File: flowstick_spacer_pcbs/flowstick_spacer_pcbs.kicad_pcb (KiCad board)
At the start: 2 copper layers, 13.6 x 40.4 mm, 0 parts

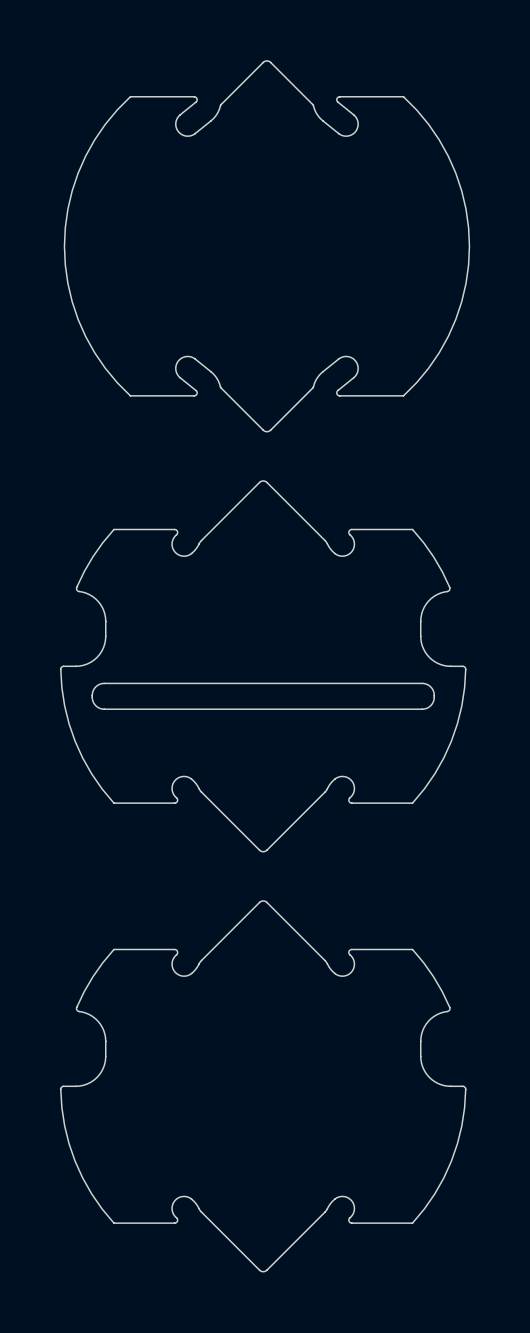
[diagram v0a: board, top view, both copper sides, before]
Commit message: work on rev2 + panelize LED strips
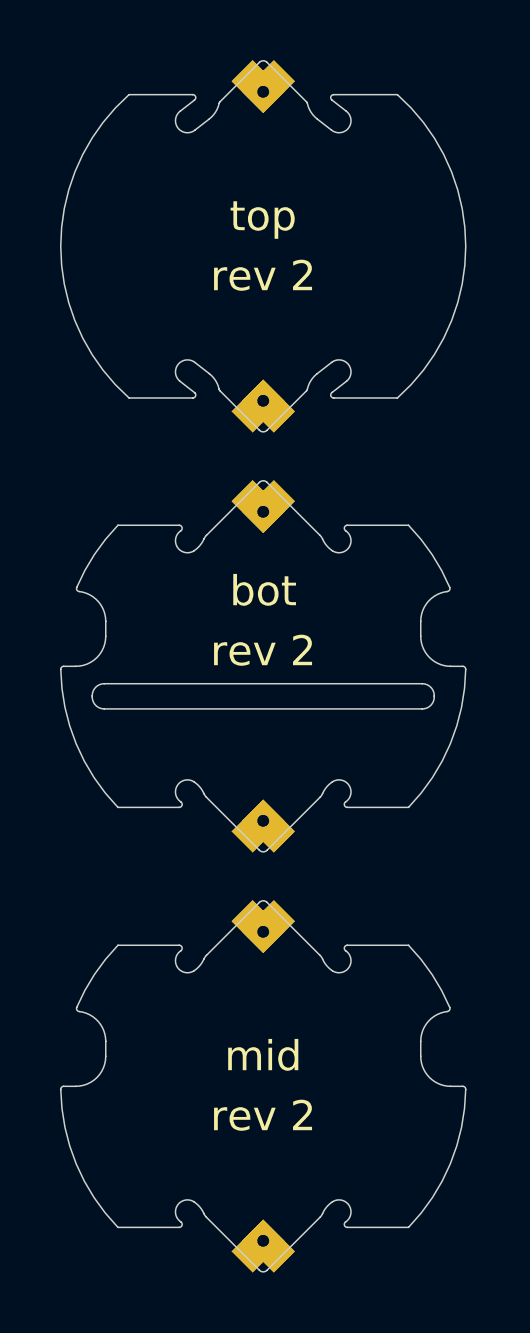
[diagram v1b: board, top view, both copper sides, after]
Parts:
- added REF**: spacer_mechanical_attachment, custom:spacer_mechanical_attachment, F.Cu at (160.0, 114.0)
- added REF**: spacer_mechanical_attachment, custom:spacer_mechanical_attachment, F.Cu at (160.0, 86.0)
- added REF**: spacer_mechanical_attachment, custom:spacer_mechanical_attachment, F.Cu at (160.0, 100.0)
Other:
- board size 13.6 x 40.4 mm -> 13.5 x 40.4 mm
- copper layers 2 -> 4
- board text added: "bot"
- board text added: "mid"
- board text added: "rev 2"
- board text added: "top"
